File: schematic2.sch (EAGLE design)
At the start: 70 parts, among them IC6 DS3231/SO

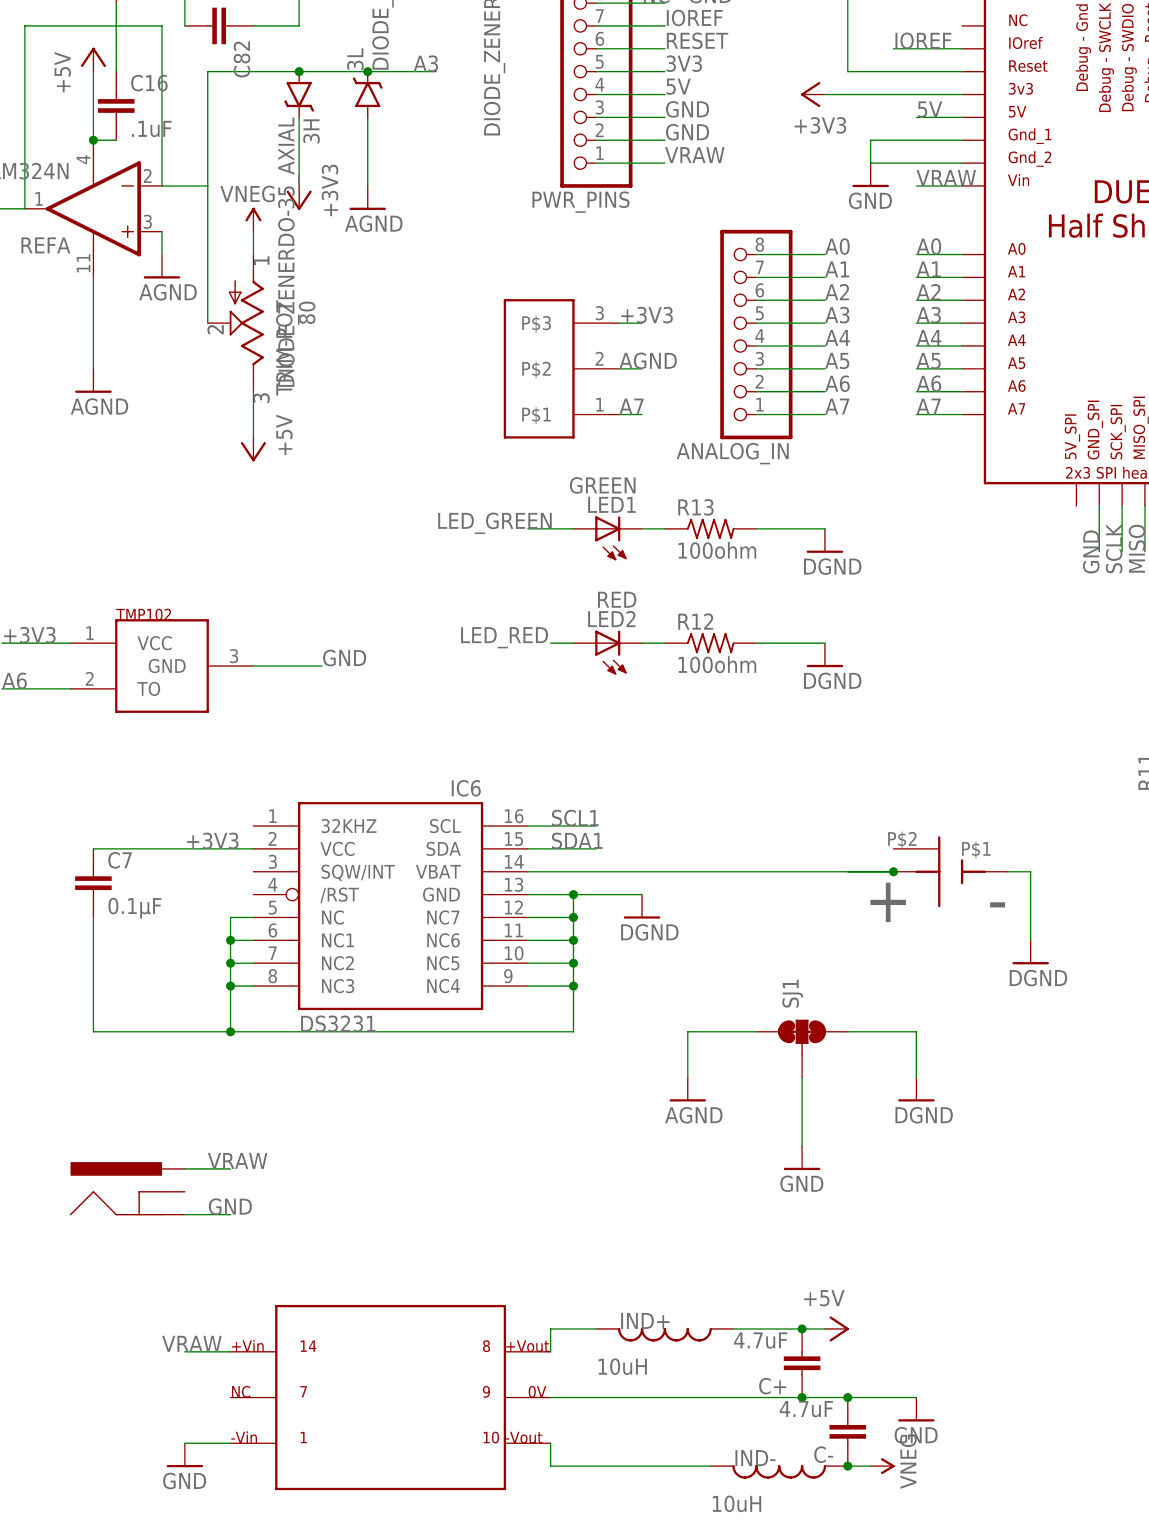
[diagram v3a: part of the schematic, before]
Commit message: Added slide switch to schematic
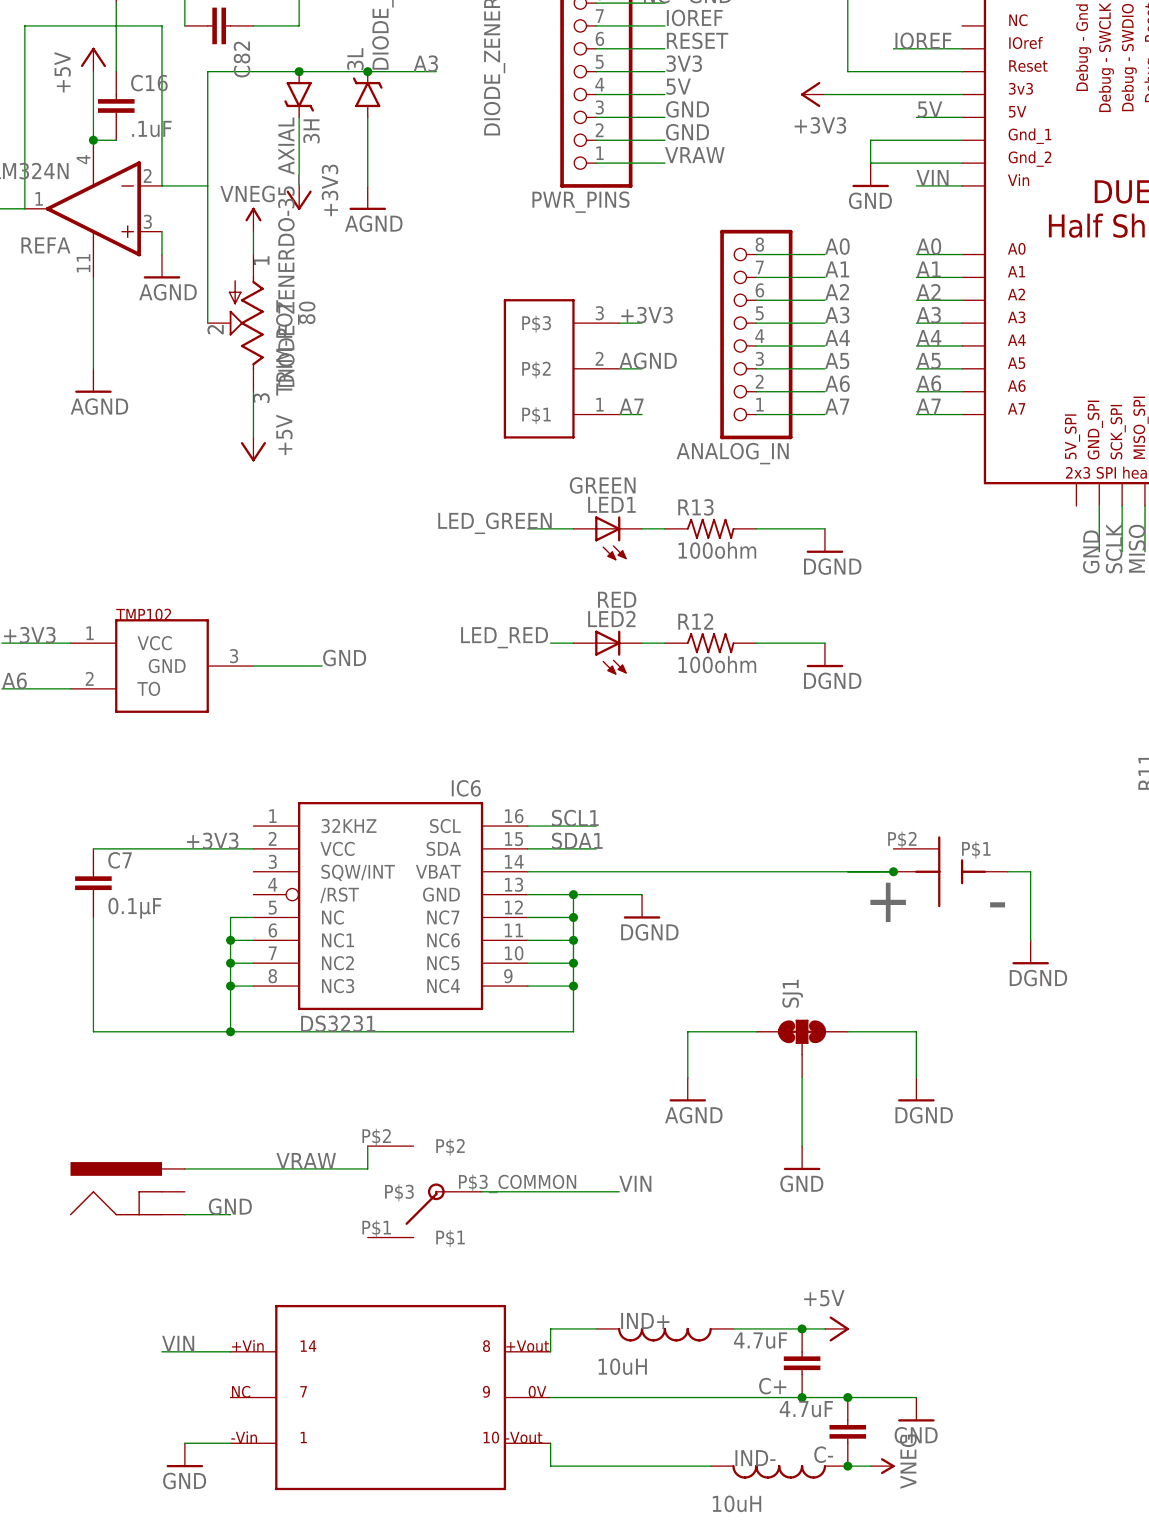
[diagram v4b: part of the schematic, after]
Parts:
- added U$2: SWITCH_SLIDE_SMD_SPDT, Felicia_force_logger:SWITCH_SLIDE_SMD_SPDT
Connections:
- new net VIN: U$1.VIN, U$2.P$3, U$3.P$14_VIN
- net VRAW: now also U$2.P$2; no longer U$1.VIN, U$3.P$14_VIN
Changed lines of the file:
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@@
 <part name="GND5" library="Felicia_force_logger" deviceset="AGND" device=""/>
 <part name="GND34" library="Felicia_force_logger" deviceset="AGND" device=""/>
+<part name="U$2" library="Felicia_force_logger" deviceset="SWITCH_SLIDE_SMD_SPDT" device=""/>
 </parts>
 <sheets>
@@
 <instance part="GND5" gate="G$1" x="162.56" y="220.98" rot="R180"/>
 <instance part="GND34" gate="G$1" x="139.7" y="172.72" rot="R180"/>
+<instance part="U$2" gate="G$1" x="175.26" y="38.1" rot="R180"/>
 </instances>
 <busses>
@@
 <net name="VRAW" class="0">
 <segment>
-<pinref part="U$3" gate="G$1" pin="P$14_VIN"/>
-<wire x1="147.32" y1="20.32" x2="152.4" y2="20.32" width="0.1524" layer="91"/>
-<label x="144.78" y="20.32" size="1.778" layer="95"/>
-</segment>
-<segment>
-<pinref part="U$28" gate="G$1" pin="PWR"/>
-<wire x1="147.32" y1="40.64" x2="152.4" y2="40.64" width="0.1524" layer="91"/>
-<label x="149.86" y="40.64" size="1.778" layer="95"/>
-</segment>
-<segment>
-<pinref part="U$1" gate="G$1" pin="VIN"/>
-<wire x1="233.68" y1="149.86" x2="228.6" y2="149.86" width="0.1524" layer="91"/>
-<label x="228.6" y="149.86" size="1.778" layer="95"/>
-</segment>
-<segment>
 <pinref part="PWR_PINS" gate="G$1" pin="1"/>
 <wire x1="193.04" y1="152.4" x2="200.66" y2="152.4" width="0.1524" layer="91"/>
 <label x="200.66" y="152.4" size="1.778" layer="95"/>
+</segment>
+<segment>
+<pinref part="U$28" gate="G$1" pin="PWR"/>
+<pinref part="U$2" gate="G$1" pin="P$2"/>
+<wire x1="147.32" y1="40.64" x2="167.64" y2="40.64" width="0.1524" layer="91"/>
+<wire x1="167.64" y1="40.64" x2="167.64" y2="43.18" width="0.1524" layer="91"/>
+<label x="157.48" y="40.64" size="1.778" layer="95"/>
 </segment>
 </net>
@@
 </segment>
 </net>
+<net name="VIN" class="0">
+<segment>
+<pinref part="U$2" gate="G$1" pin="P$3"/>
+<wire x1="180.34" y1="38.1" x2="195.58" y2="38.1" width="0.1524" layer="91"/>
+<label x="195.58" y="38.1" size="1.778" layer="95"/>
+</segment>
+<segment>
+<pinref part="U$3" gate="G$1" pin="P$14_VIN"/>
+<wire x1="152.4" y1="20.32" x2="144.78" y2="20.32" width="0.1524" layer="91"/>
+<label x="144.78" y="20.32" size="1.778" layer="95"/>
+</segment>
+<segment>
+<pinref part="U$1" gate="G$1" pin="VIN"/>
+<wire x1="233.68" y1="149.86" x2="228.6" y2="149.86" width="0.1524" layer="91"/>
+<label x="228.6" y="149.86" size="1.778" layer="95"/>
+</segment>
+</net>

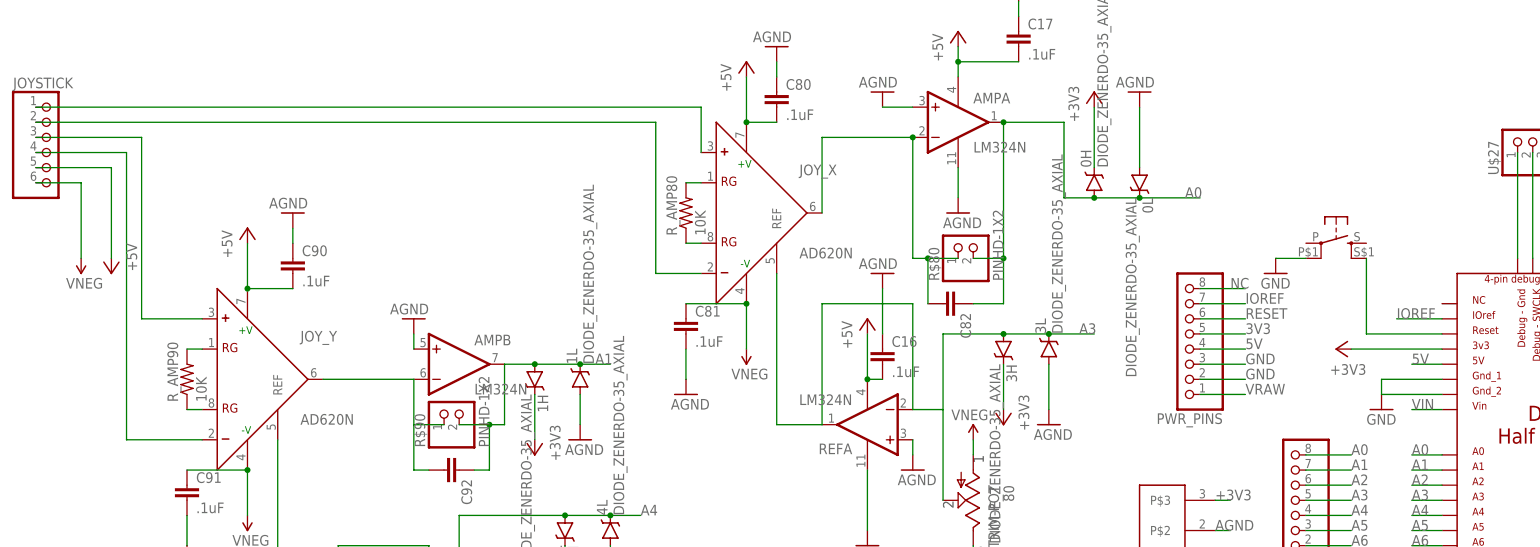
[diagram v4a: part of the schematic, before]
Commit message: Started initial routing. Swapped pins from the joystick input header to simplify routing to the in-amps.
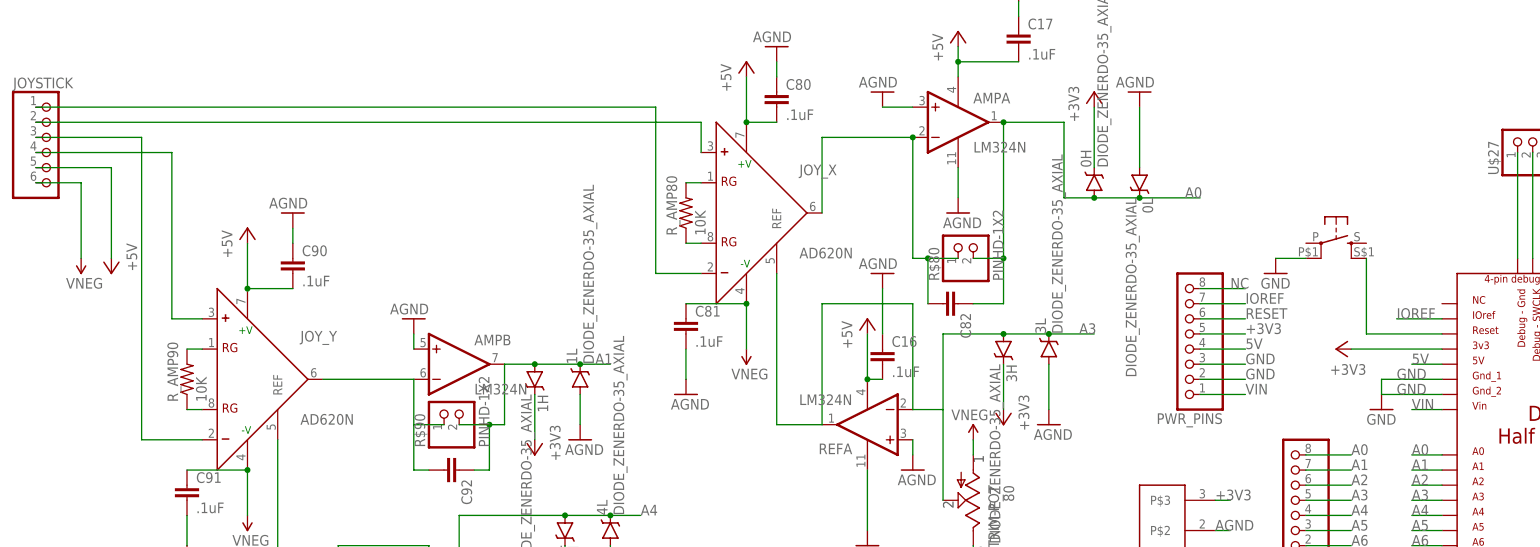
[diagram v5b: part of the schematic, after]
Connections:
- removed net 3V3: PWR_PINS.5
- removed net N$18: JOYSTICK.1, JOY_X.+
- removed net N$34: RESET.S1, U$1.RESET
- new net N$1: JOYSTICK.2, JOY_X.+
- net +3V3: now also PWR_PINS.5
- net DGND: no longer U$1.GND_1, U$1.GND_2
- net GND: now also U$1.GND_1, U$1.GND_2
- net N$19: now also JOYSTICK.1; no longer JOYSTICK.2
- net N$23: now also JOY_Y.-; no longer JOY_Y.+
- net N$24: now also JOY_Y.+; no longer JOY_Y.-
- net RESET: now also RESET.S1, U$1.RESET
- net VIN: now also PWR_PINS.1
- net VRAW: no longer PWR_PINS.1

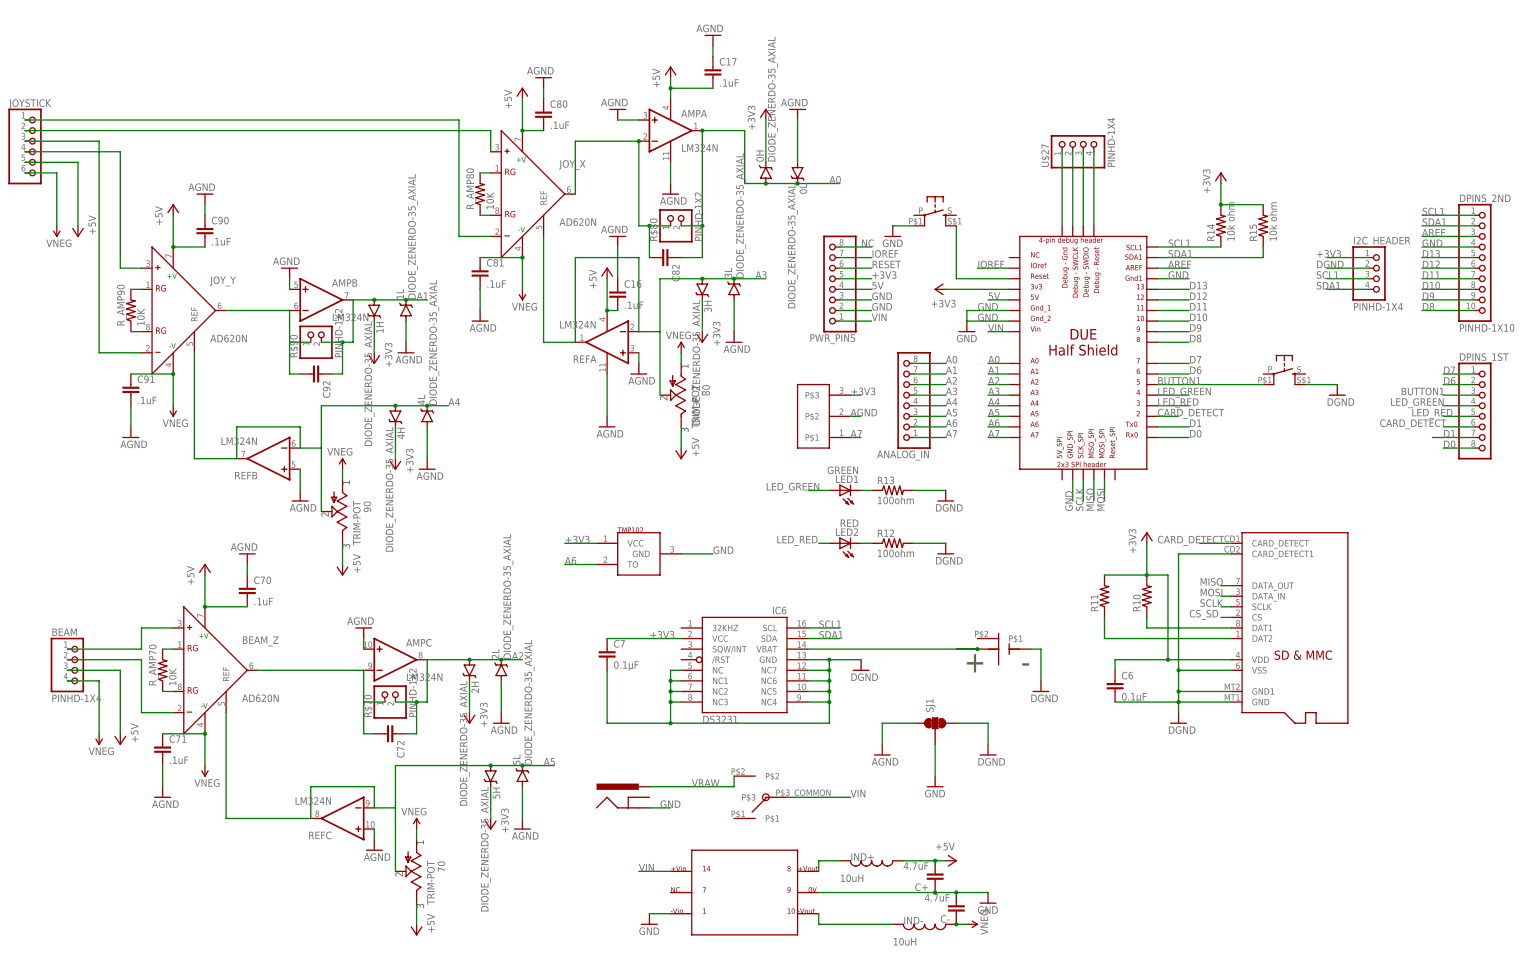
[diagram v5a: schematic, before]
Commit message: Updating some footprints and separating the analog and digital grounds.
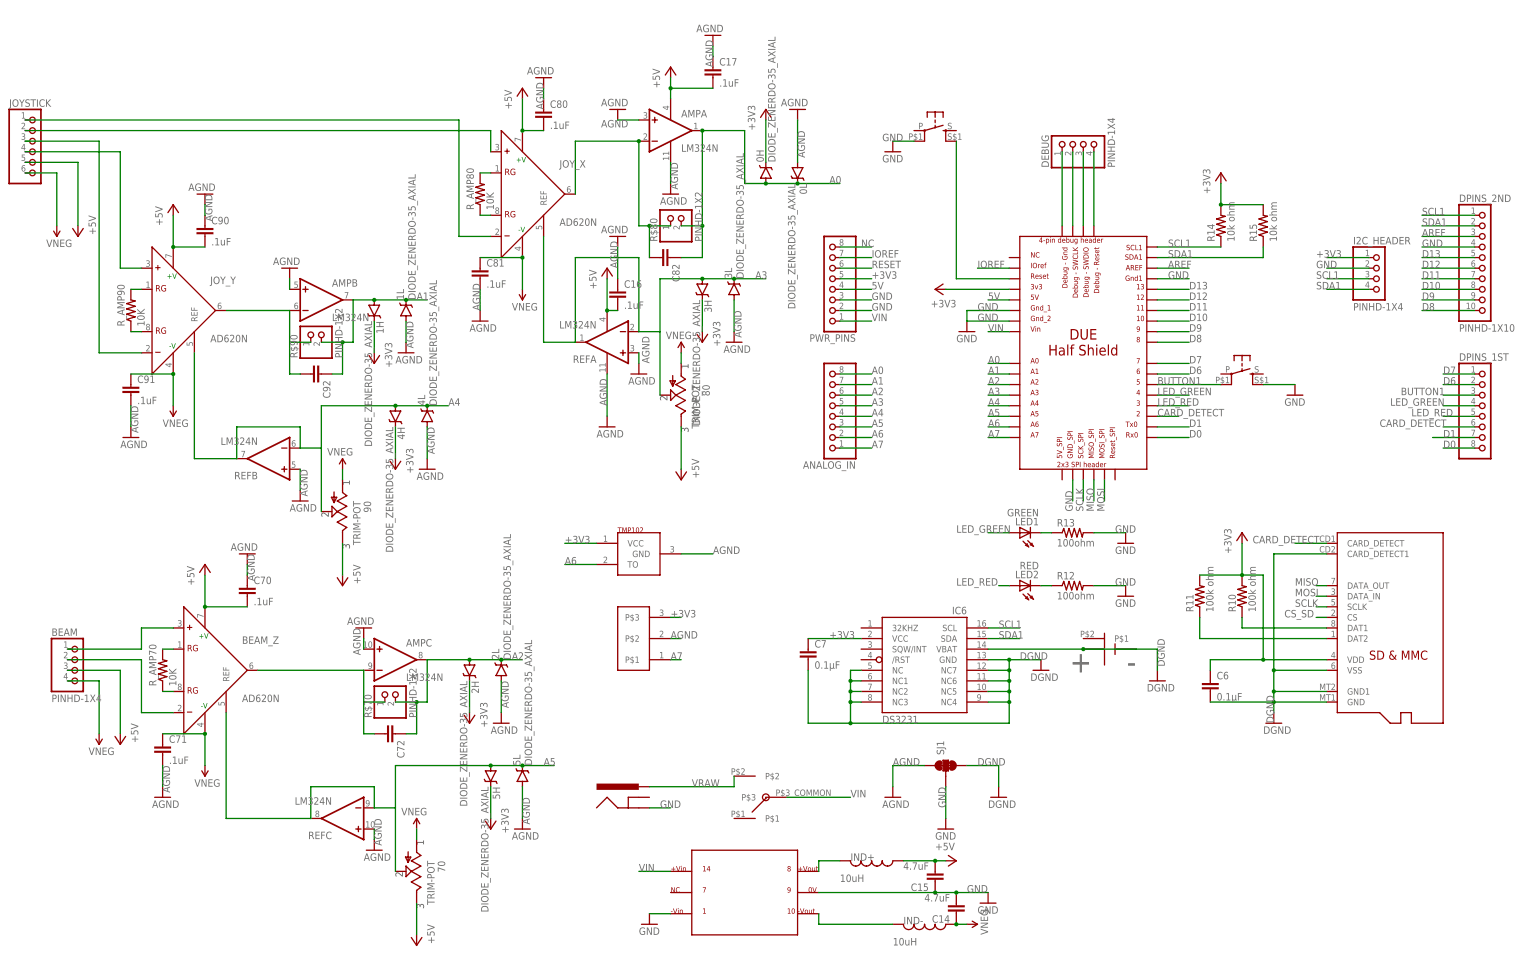
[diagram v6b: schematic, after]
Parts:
- R10, R11: value (none) -> 100k ohm
- renumbered C+ to C15, C- to C14, U$27 to DEBUG
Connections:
- net AGND: now also 1L.A, 2L.A, 4L.A, 5L.A, AMPA.+IN, AMPB.+IN, AMPC.+IN, AMPP.V-, C16.1, C17.1, C70.1, C71.2, C80.1, C81.2, C90.1, C91.2, REFA.+IN, REFB.+IN, REFC.+IN, REFP.V-, SJ1.1, TMP102.GND
- net DGND: now also SJ1.3; no longer AMPB.+IN, I2C_HEADER.2
- net GND: now also I2C_HEADER.2; no longer 1L.A, 2L.A, 4L.A, 5L.A, AMPA.+IN, AMPC.+IN, AMPP.V-, C16.1, C17.1, C70.1, C71.2, C80.1, C81.2, C90.1, C91.2, REFA.+IN, REFB.+IN, REFC.+IN, REFP.V-, SJ1.1, SJ1.3, TMP102.GND
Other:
- moved on the sheet: ANALOG_IN, C6, C7, IC6, LED1, LED2, R10, R11, R12, R13, SJ1
